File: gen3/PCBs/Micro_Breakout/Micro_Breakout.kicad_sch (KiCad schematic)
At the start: 17 parts, among them J13 SBH11-PBPC-D10-ST-BK, J7 SBH11-PBPC-D10-ST-BK, U6 Teensy4.1

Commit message: initial designs
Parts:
- removed J13, J7: SBH11-PBPC-D10-ST-BK, ImportedV2:SULLINS_SBH11-PBPC-D10-ST-BK, symbol Imported_Symbols:SBH11-PBPC-D10-ST-BK
- removed JP4, JP7: Jumper_2_Small_Open, Jumper:SolderJumper-2_P1.3mm_Open_RoundedPad1.0x1.5mm, symbol Jumper:Jumper_2_Small_Open
- removed JP41, JP49, JP50, JP51, JP52, JP53: Jumper_2_Small_Open, Connector_PinHeader_1.27mm:PinHeader_1x02_P1.27mm_Vertical, symbol Jumper:Jumper_2_Small_Open
- removed JP5, JP6: Jumper_2_Small_Bridged, Jumper:SolderJumper-2_P1.3mm_Bridged2Bar_RoundedPad1.0x1.5mm, symbol Jumper:Jumper_2_Small_Bridged
- added C6: 10uF, Capacitor_SMD:C_0805_2012Metric_Pad1.18x1.45mm_HandSolder, symbol Device:C
- added C7: 1uF, Capacitor_SMD:C_0805_2012Metric_Pad1.18x1.45mm_HandSolder, symbol Device:C
- added H10, H11, H3, H6: Molex 2 Pin Male, symbol Mechanical:MountingHole
- added H4: Molex 4 Pin Male, symbol Mechanical:MountingHole
- added J1, J11: 430450422, ImportedV2:CONN_SD-43045-008_04_MOL, symbol Imported:430450422
- added J10, J12, J13, J9: 430450228, ImportedV2:CONN_SD-43045-001_02_MOL, symbol Imported:430450228
- added J14: Conn_01x03_Pin, Connector_PinHeader_2.54mm:PinHeader_1x03_P2.54mm_Vertical, symbol Connector:Conn_01x03_Pin
- added J2: SBH11-PBPC-D05-ST-BK, Imported_Footprints:SULLINS_SBH11-PBPC-D05-ST-BK, symbol Imported:SBH11-PBPC-D05-ST-BK
- added R1, R10, R11, R2: 10k, Resistor_SMD:R_0805_2012Metric_Pad1.20x1.40mm_HandSolder, symbol Device:R_US
- added U1: BA033CC0FP-E2, ImportedV2:TO252-3_ROM, symbol Imported:BA033CC0FP-E2
- added U2: MCP9808_MSOP, Package_SO:MSOP-8_3x3mm_P0.65mm, symbol Sensor_Temperature:MCP9808_MSOP
- added U4: BME280, ImportedV2:BME280, symbol Sensor:BME280
- H7: value IDC Cable -> Molex 4 Pin Male; Supplier 1 https://www.digikey.com/en/products/detail/adafruit-industr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 -> https://www.digikey.com/en/products/detail/molex/0430250400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; Supplier 1 S/N 1528-5294-ND -> WM1784-ND
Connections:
- net UART_RX3 is gone; now on net Dled1: U6.17 (25_A11_RX6_SDA2)
- net UART_TX3 is gone; now on net Dled2: U6.16 (24_A10_TX6_SCL2)
- net +3.3V: now also C6.1, C7.1, J1.4, J10.2, J11.4, J14.2 (Pin_2), R1.1, R10.2, R11.2, R2.1, U1.3 (OUT), U2.8 (V_{DD}), U4.6 (VDDIO), U4.8 (VDD)
- net +5V: now also U1.1 (Vcc)
- net Dled1: now also J12.1; no longer U6.29 (37_CS)
- net Dled2: now also J13.1; no longer U6.28 (36_CS)
- net Dswitch1: now also J10.1
- net GND: now also C6.2, C7.2, J1.2, J11.2, J12.2, J13.2, J14.1 (Pin_1), J2.9, J9.2, U1.2 (GND), U2.4 (GND), U2.5 (A2), U2.6 (A1), U2.7 (A0), U4.1 (GND), U4.7 (GND)
- net I2C1_SCL: now also J1.3, U4.3 (SDI)
- net I2C1_SDA: now also J1.1, U4.4 (SCK)
- net Lumen_PWM: now also J9.1
- net PWM0: now also J2.1
- net PWM1: now also J2.3
- net PWM2: now also J2.5
- net PWM3: now also J2.7
- net PWM4: now also J2.2
- net PWM5: now also J2.4
- net PWM6: now also J2.6
- net PWM7: now also J2.8
- net UART_RX2: now also J11.1, R11.1
- net UART_TX2: now also J11.3, R10.1
- net xDleak: now also J14.3 (Pin_3)
- net Analog_Current renamed PIN41
- net Analog_Voltage renamed PIN40
- net DISP_DC renamed PIN31
- net DISP_LED renamed PIN32
- net DISP_RST renamed PIN30
- net Device_D+: no longer names the net of U6.67 (D+)
- net Device_D-: no longer names the net of U6.66 (D-)
- net D/A14 renamed PIN14
- net D/A20 renamed PIN20
- net D/A21 renamed PIN21
- net D/A22 renamed PIN22
- net D/A23 renamed PIN23
- net ETH_GND: no longer names the net of U6.64 (GND)
- net GPIOExp_INT renamed PIN15
- net Host_D+: no longer names the net of U6.57 (D+)
- net Host_D-: no longer names the net of U6.56 (D-)
- net LED: no longer names the net of U6.61 (LED)
- net R+: no longer names the net of U6.60 (R+)
- net R-: no longer names the net of U6.65 (R-)
- net T+: no longer names the net of U6.63 (T+)
- net T-: no longer names the net of U6.62 (T-)
- net toNEO_CTRL_ESCs renamed PIN9
- net toNEO_CTRL_EXTs renamed PIN38
- net toNEO_CTRL_MLU renamed PIN39
- net toNEO_CTRL_Orin renamed PIN33
- new net: R2.2, U4.2 (CSB)
- new net: R1.2, U4.5 (SDO)
- new net PIN36: U6.28 (36_CS)
- new net PIN37: U6.29 (37_CS)
- no-connect marks 14 -> 23
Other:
- removed sheet GPIO_Expander
- removed sheet Neopixels
- removed sheet On-board Sensors
- removed sheet Peripheral Connectors
- removed sheet Power Management
- note added: "3.3V, 1A output"
- note added: "5V --> 3.3V Reg"
- note added: "BlueRobotics Depth Sensor I2C @ 0x76"
- note added: "Bulkhead LEDs"
- note added: "External Sensors"
- note added: "Hardware/Software Kill Switch"
- note added: "I2C @ 0x18 format: 0011(A2)(A1)(A0)"
- note added: "I2C @ 0x76 when SDO low *I2C @ 0x77 when SDO high"
- note added: "Integrated BME280 (Humidity, Pressure)"
- note added: "Integrated MCP9808 (Temperature)"
- note added: "Interconnect to ESC Board (10 pin)"
- note added: "Internal Sensors"
- note added: "Lumen LED PWM"
- note added: "Power Regulation"
- note added: "SPI Bus"
- note added: "StarOddi CTD Comms over 2nd UART Bus"
- note added: "socket here + leave space to mount"
- note removed: "5V Orin-->MLU Orin requires own 5V --> 3.3V converter"
- note removed: "Arm Host"
- note removed: "Display"
- note removed: "Display Interface"
- note removed: "Interconnect to ESC Board"
- note removed: "Interconnect to Orin"
- note removed: "Interrupt to GPIO Expander"
- note removed: "Neos"
- note removed: "Orin Interconnects"
- note removed: "Pixhawk IN"
- note removed: "Solder resistors onto jumpers if voltage division is necessary"
- note removed: "Teensy Device"
- note removed: "UART Arm"
- moved on the sheet: H5, R4, R5, U6

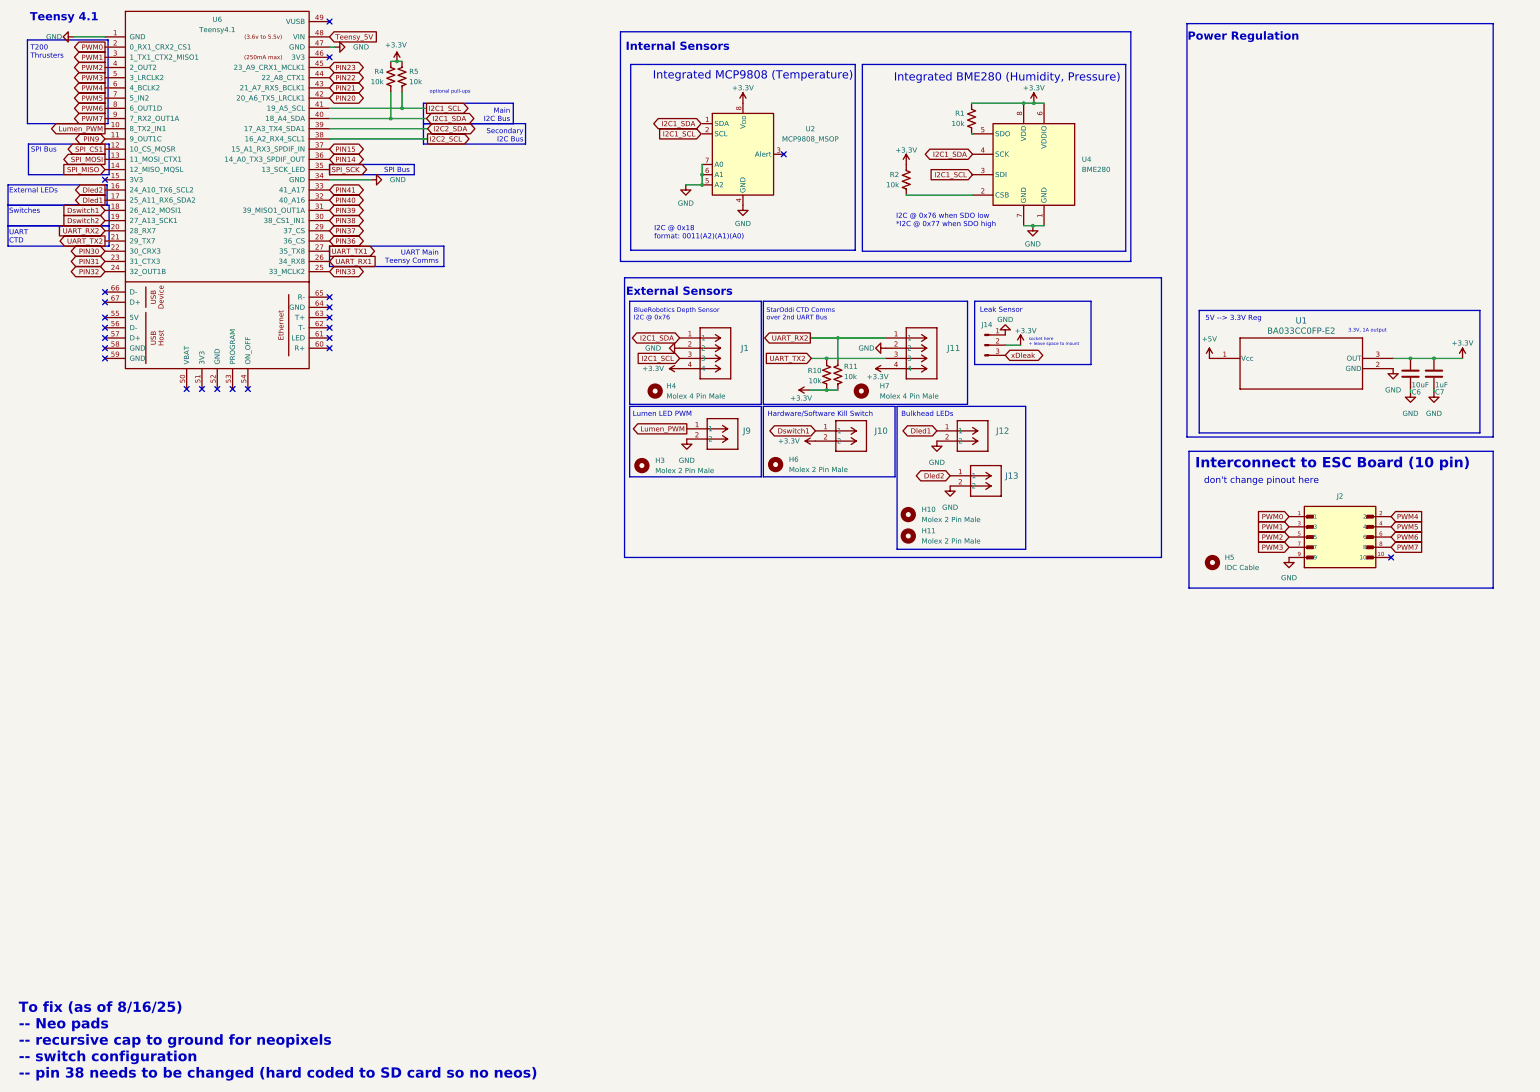
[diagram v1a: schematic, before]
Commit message: schematics of microboard done
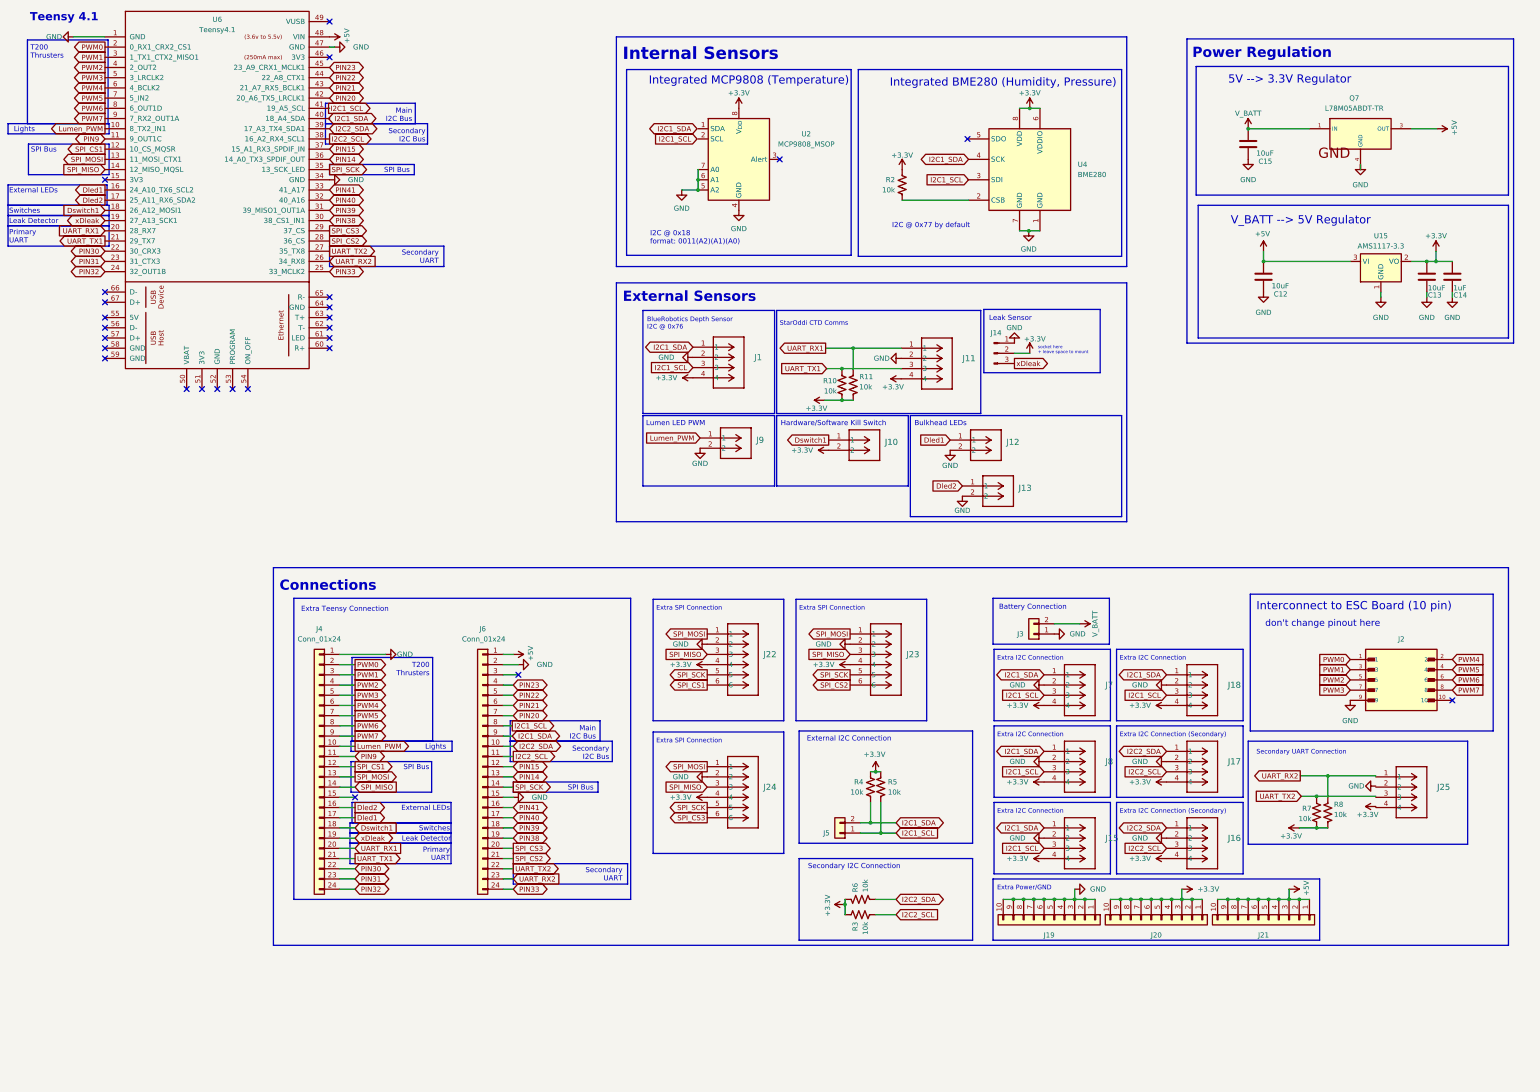
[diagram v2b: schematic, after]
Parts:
- removed C6: 10uF, Capacitor_SMD:C_0805_2012Metric_Pad1.18x1.45mm_HandSolder, symbol Device:C
- removed C7: 1uF, Capacitor_SMD:C_0805_2012Metric_Pad1.18x1.45mm_HandSolder, symbol Device:C
- removed H10, H11, H3, H6: Molex 2 Pin Male, symbol Mechanical:MountingHole
- removed H4, H7: Molex 4 Pin Male, symbol Mechanical:MountingHole
- removed H5: IDC Cable, symbol Mechanical:MountingHole
- removed R1: 10k, Resistor_SMD:R_0805_2012Metric_Pad1.20x1.40mm_HandSolder, symbol Device:R_US
- removed U1: BA033CC0FP-E2, ImportedV2:TO252-3_ROM, symbol Imported:BA033CC0FP-E2
- added C12, C13, C15: 10uF, Capacitor_SMD:C_0805_2012Metric_Pad1.18x1.45mm_HandSolder, symbol Device:C
- added C14: 1uF, Capacitor_SMD:C_0805_2012Metric_Pad1.18x1.45mm_HandSolder, symbol Device:C
- added J15, J16, J17, J18, J25, J7, J8: 430450422, Imported_Footprints:CONN_SD-43045-005_04_MOL, symbol Imported:430450422
- added J19, J20, J21: Conn_01x10, Connector_PinHeader_2.54mm:PinHeader_1x10_P2.54mm_Vertical, symbol Connector_Generic:Conn_01x10
- added J22, J23, J24: 430450612, Imported_Footprints:CONN_SD-43045-005_06_MOL, symbol CONN_SD-43045-008_06_MOL:430450612
- added J3: Battery, Connector_AMASS:AMASS_XT60PW-F_1x02_P7.20mm_Horizontal, symbol Connector_Generic:Conn_01x02
- added J4, J6: Conn_01x24, Connector_PinHeader_2.54mm:PinHeader_1x24_P2.54mm_Vertical, symbol Connector_Generic:Conn_01x24
- added J5: Battery, Connector_AMASS:AMASS_XT30PW-F_1x02_P2.50mm_Horizontal, symbol Connector_Generic:Conn_01x02
- added Q7: L78M05ABDT-TR, robosub_footprints:TO-252-2_L6.5-W6.1-P4.58-LS10.0-TL, symbol L78M05ABDT-TR:L78M05ABDT-TR
- added R3, R6, R7, R8: 10k, Resistor_SMD:R_0805_2012Metric_Pad1.20x1.40mm_HandSolder, symbol Device:R_US
- added U15: AMS1117-3.3, Package_TO_SOT_SMD:SOT-223-3_TabPin2, symbol Regulator_Linear:AMS1117-3.3
- J1, J11: footprint ImportedV2:CONN_SD-43045-008_04_MOL -> Imported_Footprints:CONN_SD-43045-005_04_MOL
- J10, J12, J13, J9: footprint ImportedV2:CONN_SD-43045-001_02_MOL -> Imported_Footprints:CONN_SD-43045-005_02_MOL
- U4: footprint ImportedV2:BME280 -> Package_LGA:Bosch_LGA-8_2.5x2.5mm_P0.65mm_ClockwisePinNumbering
- U6: footprint Module:Teensy41 -> Imported_Footprints:Teensy41
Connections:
- net Dswitch2 is gone; now on net xDleak: U6.19 (27_A13_SCK1)
- net Teensy_5V is gone; now on net +5V: U6.48 (VIN)
- net +3.3V: now also C13.1, C14.1, J15.4, J16.4, J17.4, J18.4, J20.1 (Pin_1), J20.10 (Pin_10), J20.2 (Pin_2), J20.3 (Pin_3), J20.4 (Pin_4), J20.5 (Pin_5), J20.6 (Pin_6), J20.7 (Pin_7), J20.8 (Pin_8), J20.9 (Pin_9), J22.4, J23.4, J24.4, J7.4, J8.4, R3.1, R6.1, R7.2, R8.2, U15.2 (VO)
- net +5V: now also C12.1, J21.1 (Pin_1), J21.10 (Pin_10), J21.2 (Pin_2), J21.3 (Pin_3), J21.4 (Pin_4), J21.5 (Pin_5), J21.6 (Pin_6), J21.7 (Pin_7), J21.8 (Pin_8), J21.9 (Pin_9), J6.1 (Pin_1), Q7.3 (OUT), U15.3 (VI)
- net Dled1: now also U6.16 (24_A10_TX6_SCL2), J4.17 (Pin_17); no longer U6.17 (25_A11_RX6_SDA2)
- net Dled2: now also U6.17 (25_A11_RX6_SDA2), J4.16 (Pin_16); no longer U6.16 (24_A10_TX6_SCL2)
- net Dswitch1: now also J4.18 (Pin_18)
- net GND: now also C12.2, C13.2, C14.2, C15.2, J15.2, J16.2, J17.2, J18.2, J19.1 (Pin_1), J19.10 (Pin_10), J19.2 (Pin_2), J19.3 (Pin_3), J19.4 (Pin_4), J19.5 (Pin_5), J19.6 (Pin_6), J19.7 (Pin_7), J19.8 (Pin_8), J19.9 (Pin_9), J22.2, J23.2, J24.2, J3.1 (Pin_1), J4.1 (Pin_1), J6.15 (Pin_15), J6.2 (Pin_2), J7.2, J8.2, Q7.4 (GND), U15.1 (GND)
- net I2C1_SCL: now also J15.3, J18.3, J5.1 (Pin_1), J6.8 (Pin_8), J7.3, J8.3
- net I2C1_SDA: now also J15.1, J18.1, J5.2 (Pin_2), J6.9 (Pin_9), J7.1, J8.1
- net I2C2_SCL: now also J16.3, J17.3, J6.11 (Pin_11), R3.2
- net I2C2_SDA: now also J16.1, J17.1, J6.10 (Pin_10), R6.2
- net Lumen_PWM: now also J4.10 (Pin_10)
- net PIN14: now also J6.13 (Pin_13)
- net PIN15: now also J6.12 (Pin_12)
- net PIN20: now also J6.7 (Pin_7)
- net PIN21: now also J6.6 (Pin_6)
- net PIN22: now also J6.5 (Pin_5)
- net PIN23: now also J6.4 (Pin_4)
- net PIN30: now also J4.22 (Pin_22)
- net PIN31: now also J4.23 (Pin_23)
- net PIN32: now also J4.24 (Pin_24)
- net PIN33: now also J6.24 (Pin_24)
- net PIN38: now also J6.19 (Pin_19)
- net PIN39: now also J6.18 (Pin_18)
- net PIN40: now also J6.17 (Pin_17)
- net PIN41: now also J6.16 (Pin_16)
- net PIN9: now also J4.11 (Pin_11)
- net PWM0: now also J4.2 (Pin_2)
- net PWM1: now also J4.3 (Pin_3)
- net PWM2: now also J4.4 (Pin_4)
- net PWM3: now also J4.5 (Pin_5)
- net PWM4: now also J4.6 (Pin_6)
- net PWM5: now also J4.7 (Pin_7)
- net PWM6: now also J4.8 (Pin_8)
- net PWM7: now also J4.9 (Pin_9)
- net SPI_CS1: now also J22.6, J4.12 (Pin_12)
- net SPI_MISO: now also J22.3, J23.3, J24.3, J4.14 (Pin_14)
- net SPI_MOSI: now also J22.1, J23.1, J24.1, J4.13 (Pin_13)
- net SPI_SCK: now also J22.5, J23.5, J24.5, J6.14 (Pin_14)
- net UART_RX1: now also J11.1, R11.1, U6.20 (28_RX7), J4.20 (Pin_20); no longer U6.26 (34_RX8)
- net UART_RX2: now also U6.26 (34_RX8), J6.23 (Pin_23), R8.1; no longer J11.1, R11.1, U6.20 (28_RX7)
- net UART_TX1: now also J11.3, R10.1, U6.21 (29_TX7), J4.21 (Pin_21); no longer U6.27 (35_TX8)
- net UART_TX2: now also U6.27 (35_TX8), J6.22 (Pin_22), R7.1; no longer J11.3, R10.1, U6.21 (29_TX7)
- net xDleak: now also J4.19 (Pin_19)
- net PIN36 renamed SPI_CS2
- net SPI_CS2: now also J23.6, J6.21 (Pin_21)
- net PIN37 renamed SPI_CS3
- net SPI_CS3: now also J24.6, J6.20 (Pin_20)
- new net V_BATT: C15.1, J3.2 (Pin_2), Q7.1 (IN)
- no-connect marks 23 -> 26
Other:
- note added: "5V --> 3.3V Regulator"
- note added: "Battery Connection"
- note added: "Connections"
- note added: "External I2C Connection"
- note added: "Extra I2C Connection"
- note added: "Extra I2C Connection (Secondary)"
- note added: "Extra Power/GND"
- note added: "Extra SPI Connection"
- note added: "Extra Teensy Connection"
- note added: "I2C @ 0x77 by default"
- note added: "Leak Detector"
- note added: "Lights"
- note added: "Primary UART"
- note added: "Secondary I2C Connection"
- note added: "Secondary UART"
- note added: "Secondary UART Connection"
- note added: "StarOddi CTD Comms"
- note added: "V_BATT --> 5V Regulator"
- note removed: "3.3V, 1A output"
- note removed: "5V --> 3.3V Reg"
- note removed: "I2C @ 0x76 when SDO low *I2C @ 0x77 when SDO high"
- note removed: "StarOddi CTD Comms over 2nd UART Bus"
- note removed: "To fix (as of 8/16/25) -- Neo pads -- recursive cap to ground for neopixels -- switch configuration -- pin 38 needs to be changed (hard coded to SD card so no neos)"
- note removed: "UART CTD"
- note removed: "UART Main Teensy Comms"
- note removed: "optional pull-ups"
- title: Main Logic Unit Breakout -> Main Microcontroller Breakout Board
- moved on the sheet: J1, J14, J2, J9, R10, R11, R2, R4, R5, U2, U4

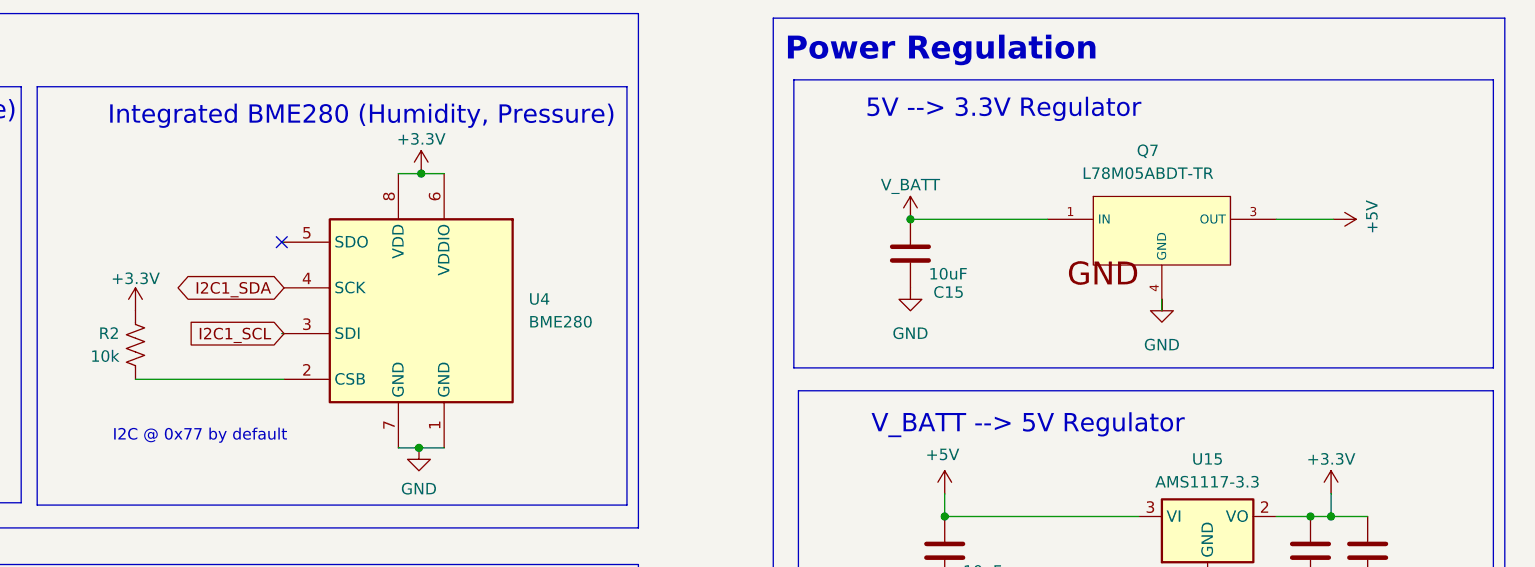
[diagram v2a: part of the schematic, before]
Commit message: added caps to micro breakout
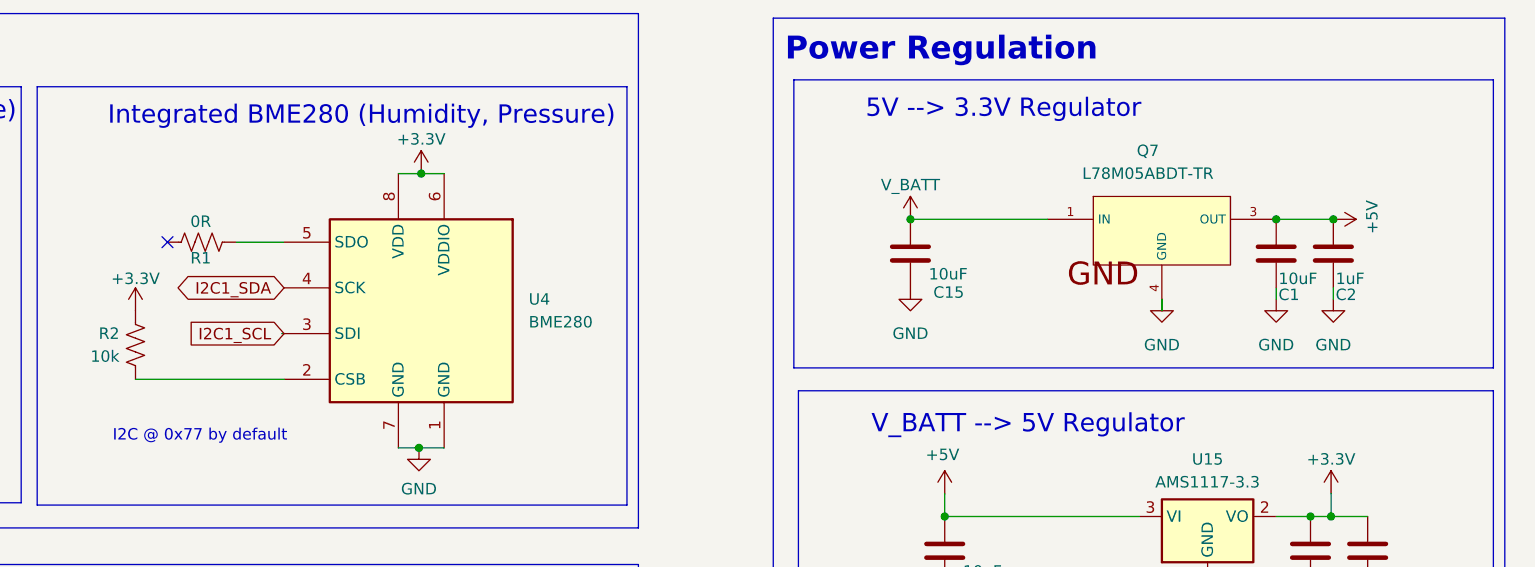
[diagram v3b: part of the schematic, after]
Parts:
- added C1: 10uF, Capacitor_SMD:C_0805_2012Metric_Pad1.18x1.45mm_HandSolder, symbol Device:C
- added C2: 1uF, Capacitor_SMD:C_0805_2012Metric_Pad1.18x1.45mm_HandSolder, symbol Device:C
- added R1: 0R, Resistor_SMD:R_0805_2012Metric_Pad1.20x1.40mm_HandSolder, symbol Device:R_US
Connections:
- net +5V: now also C1.1, C2.1
- net GND: now also C1.2, C2.2
- net at U4.5 (SDO): now also R1.2
